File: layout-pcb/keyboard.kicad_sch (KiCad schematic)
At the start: 276 parts

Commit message: pcb basic wiring
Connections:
- net 26p4-27p2: no longer D27.4 (DIN), D28.2 (DOUT)
- net at D66.2 (DOUT): now also D67.4 (DIN)
- net 50p2-66p4: now reaches D66.4 (DIN)
- net 50p2-66p4: now also D50.2 (DOUT)
- net at D69.2 (DOUT): now also D70.4 (DIN)
- net at D69.4 (DIN): now also D68.2 (DOUT)
- net at D92.2 (DOUT): now also D93.4 (DIN)
- net LED-Status IN: now reaches D92.4 (DIN)
- net at D58.2 (DOUT): now also D57.4 (DIN)
- net at D58.4 (DIN): now also D59.2 (DOUT)
- net at D34.2 (DOUT): now also D35.4 (DIN)
- net at D34.4 (DIN): now also D33.2 (DOUT)
- net at D40.2 (DOUT): now also D41.4 (DIN)
- net 39p2-40p4: now reaches D40.4 (DIN)
- net 39p2-40p4: now also D39.2 (DOUT)
- net at D56.2 (DOUT): now also D55.4 (DIN)
- net at D56.4 (DIN): now also D57.2 (DOUT)
- net at D43.2 (DOUT): now also D44.4 (DIN)
- net at D43.4 (DIN): now also D42.2 (DOUT)
- net at D48.2 (DOUT): now also D49.4 (DIN)
- net at D48.4 (DIN): now also D47.2 (DOUT)
- net at D47.4 (DIN): now also D46.2 (DOUT)
- net at D62.2 (DOUT): now also D61.4 (DIN)
- net at D62.4 (DIN): now also D63.2 (DOUT)
- net at D90.2 (DOUT): now also D89.4 (DIN)
- net at D90.4 (DIN): now also D91.2 (DOUT)
- net at D75.2 (DOUT): now also D76.4 (DIN)
- net at D75.4 (DIN): now also D74.2 (DOUT)
- net at D87.2 (DOUT): now also D86.4 (DIN)
- net at D87.4 (DIN): now also D88.2 (DOUT)
- net at D74.4 (DIN): now also D73.2 (DOUT)
- net at D67.2 (DOUT): now also D68.4 (DIN)
- net at D55.2 (DOUT): now also D54.4 (DIN)
- net at D60.2 (DOUT): now also D59.4 (DIN)
- net at D60.4 (DIN): now also D61.2 (DOUT)
- net at D76.2 (DOUT): now also D77.4 (DIN)
- net at D72.2 (DOUT): now also D73.4 (DIN)
- net at D72.4 (DIN): now also D71.2 (DOUT)
- net at D52.2 (DOUT): now also D51.4 (DIN)
- net 53p2-52p4: now reaches D52.4 (DIN)
- net 53p2-52p4: now also D53.2 (DOUT)
- net at D44.2 (DOUT): now also D45.4 (DIN)
- net at D42.4 (DIN): now also D41.2 (DOUT)
- net at D51.2 (DOUT): now also D50.4 (DIN)
- net 81p2-91p4: now reaches D91.4 (DIN)
- net 81p2-91p4: now also D81.2 (DOUT)
- net at D85.2 (DOUT): now also D84.4 (DIN)
- net at D85.4 (DIN): now also D86.2 (DOUT)
- net at D37.2 (DOUT): now also D38.4 (DIN)
- net at D37.4 (DIN): now also D36.2 (DOUT)
- net at D93.2 (DOUT): now also D94.4 (DIN)
- net at D33.4 (DIN): now also D32.2 (DOUT)
- net at D79.2 (DOUT): now also D80.4 (DIN)
- net 78p2-79p4: now reaches D79.4 (DIN)
- net 78p2-79p4: now also D78.2 (DOUT)
- net at D88.4 (DIN): now also D89.2 (DOUT)
- net at D36.4 (DIN): now also D35.2 (DOUT)
- net at D82.4 (DIN): now also D83.2 (DOUT)
- net at D46.4 (DIN): now also D45.2 (DOUT)
- net at D65.2 (DOUT): now also D64.4 (DIN)
- net 49p2-65p4: now reaches D65.4 (DIN)
- net 49p2-65p4: now also D49.2 (DOUT)
- net at D78.4 (DIN): now also D77.2 (DOUT)
- net at D70.2 (DOUT): now also D71.4 (DIN)
- net at D63.4 (DIN): now also D64.2 (DOUT)
- net at D53.4 (DIN): now also D54.2 (DOUT)
- net at D39.4 (DIN): now also D38.2 (DOUT)
- net 14p2-32p4: now reaches D14.2 (DOUT)
- net 14p2-32p4: now also D32.4 (DIN)
- net at D83.4 (DIN): now also D84.2 (DOUT)
- net at D80.2 (DOUT): now also D81.4 (DIN)
- new net: D27.4 (DIN), D28.2 (DOUT)

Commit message: update
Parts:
- removed D1, D10, D11, D12, D13, D14, D15, D16, D17, D18, D19, D2, D20, D21, D22, D23, D24, D25, D26, D27, D28, D29, D3, D30, D31, D32, D33, D34, D35, D36, D37, D38, D39, D4, D40, D41, D42, D43, D44, D45, D46, D47, D48, D49, D5, D50, D51, D52, D53, D54, D55, D56, D57, D58, D59, D6, D60, D61, D62, D63, D64, D65, D66, D67, D68, D69, D7, D70, D71, D72, D73, D74, D75, D76, D77, D78, D79, D8, D80, D81, D82, D83, D84, D85, D86, D87, D88, D89, D9, D90, D91, D92, D93, D94: WS2812B, LED_SMD:LED_WS2812B_PLCC4_5.0x5.0mm_P3.2mm, symbol LED:WS2812B
- D_0, D_1, D_10, D_11, D_12, D_13, D_14, D_15, D_16, D_17, D_18, D_19, D_2, D_20, D_21, D_22, D_23, D_24, D_25, D_26, D_27, D_28, D_29, D_3, D_30, D_31, D_32, D_33, D_34, D_35, D_36, D_37, D_38, D_39, D_4, D_40, D_41, D_42, D_43, D_44, D_45, D_46, D_47, D_48, D_49, D_5, D_50, D_51, D_52, D_53, D_54, D_55, D_56, D_57, D_58, D_59, D_6, D_60, D_61, D_62, D_63, D_64, D_65, D_66, D_67, D_68, D_69, D_7, D_70, D_71, D_72, D_73, D_74, D_75, D_76, D_77, D_78, D_79, D_8, D_80, D_81, D_82, D_83, D_84, D_85, D_86, D_87, D_88, D_89, D_9, D_90: Mouser (none) -> 485-5099
- K_13, K_14, K_15, K_16, K_17, K_18, K_19, K_20, K_21, K_22, K_23, K_24, K_25, K_26, K_27, K_28, K_29, K_30, K_31, K_32, K_33, K_34, K_35, K_36, K_37, K_38, K_39, K_40, K_41, K_42, K_43, K_44, K_45, K_46, K_47, K_48, K_49, K_50, K_51, K_52, K_53, K_54, K_55, K_56, K_57, K_58, K_59, K_60, K_61, K_62, K_63, K_64, K_65, K_66, K_67, K_68, K_69, K_70, K_71, K_72, K_73, K_74, K_75, K_76, K_77, K_78, K_79, K_80, K_81, K_82, K_83, K_84, K_85, K_86, K_87, K_88, K_89, K_90, K_ESC1, K_F1, K_F10, K_F11, K_F12, K_F2, K_F3, K_F4, K_F5, K_F6, K_F7, K_F8, K_F9: Mouser (none) -> 540-MX1A-E1NN
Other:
- added sheet Controler (untitled.kicad_sch)
- added sheet LED Matrix (untitled.kicad_sch)
- company: (none) -> JJW Inc.
- title: (none) -> No Arrows

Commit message: update
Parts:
- added D1, D10, D11, D12, D13, D14, D15, D16, D17, D18, D19, D2, D20, D21, D22, D23, D24, D25, D26, D27, D28, D29, D3, D30, D31, D32, D33, D34, D35, D36, D37, D38, D39, D4, D40, D41, D42, D43, D44, D45, D46, D47, D48, D49, D5, D50, D51, D52, D53, D54, D55, D56, D57, D58, D59, D6, D60, D61, D62, D63, D64, D65, D66, D67, D68, D69, D7, D70, D71, D72, D73, D74, D75, D76, D77, D78, D79, D8, D80, D81, D82, D83, D84, D85, D86, D87, D88, D89, D9, D90, D91, D92, D93, D94: WS2812B, LED_SMD:LED_WS2812B_PLCC4_5.0x5.0mm_P3.2mm, symbol LED:WS2812B
- added J1: USB_C_Receptacle_USB2.0_16P, Connector_USB:USB_C_Receptacle_GCT_USB4110, symbol Connector:USB_C_Receptacle_USB2.0_16P
- added R1, R2: 5K1, Resistor_SMD:R_2010_5025Metric_Pad1.40x2.65mm_HandSolder, symbol Device:R
- added SW1: 3983, kb2040:SW_3983_ADA, symbol 2024-11-03_10-00-00:3983
- added U1: RP2040_Stamp, kb2040:RP2xxx_Stamp_SMD, symbol RP2xxx_Stamp:RP2040_Stamp
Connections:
- net col0: now also U1.30 (GPIO29)
- net col1: now also U1.29 (GPIO28)
- net col10: now also U1.19 (GPIO18)
- net col11: now also U1.18 (GPIO17)
- net col12: now also U1.17 (GPIO16)
- net col13: now also U1.16 (GPIO15)
- net col14: now also U1.15 (GPIO14)
- net col15: now also U1.14 (GPIO13)
- net col16: now also U1.13 (GPIO12)
- net col17: now also U1.12 (GPIO11)
- net col18: now also U1.11 (GPIO10)
- net col2: now also U1.28 (GPIO27)
- net col3: now also U1.27 (GPIO26)
- net col4: now also U1.26 (GPIO25)
- net col5: now also U1.25 (GPIO24)
- net col6: now also U1.24 (GPIO23)
- net col7: now also U1.23 (GPIO22)
- net col8: now also U1.22 (GPIO21)
- net col9: now also U1.21 (GPIO20)
- net row0: now also U1.10 (GPIO9)
- net row1: now also U1.9 (GPIO8)
- net row2: now also U1.8 (GPIO7)
- net row3: now also U1.7 (GPIO6)
- net row4: now also U1.6 (GPIO5)
- net row5: now also U1.5 (GPIO4)
- new net: D6.2 (DOUT), D7.4 (DIN)
- new net: D5.2 (DOUT), D6.4 (DIN)
- new net: D7.2 (DOUT), D8.4 (DIN)
- new net: D23.4 (DIN), D24.2 (DOUT)
- new net: D24.4 (DIN), D25.2 (DOUT)
- new net: D66.2 (DOUT), D67.4 (DIN)
- new net: D17.4 (DIN), D18.2 (DOUT)
- new net: D18.4 (DIN), D19.2 (DOUT)
- new net: J1.A5 (CC1), R1.1
- new net: J1.A4 (VBUS), J1.A9 (VBUS), J1.B4 (VBUS), J1.B9 (VBUS), R1.2, R2.2, U1.33 (5V)
- new net: D69.2 (DOUT), D70.4 (DIN)
- new net: D68.2 (DOUT), D69.4 (DIN)
- new net: D92.2 (DOUT), D93.4 (DIN)
- new net: D57.4 (DIN), D58.2 (DOUT)
- new net: D58.4 (DIN), D59.2 (DOUT)
- new net: D11.2 (DOUT), D12.4 (DIN)
- new net: D10.2 (DOUT), D11.4 (DIN)
- new net: D34.2 (DOUT), D35.4 (DIN)
- new net: D33.2 (DOUT), D34.4 (DIN)
- new net: D29.4 (DIN), D30.2 (DOUT)
- new net: D30.4 (DIN), D31.2 (DOUT)
- new net: D27.4 (DIN), D28.2 (DOUT)
- new net: D40.2 (DOUT), D41.4 (DIN)
- new net: D55.4 (DIN), D56.2 (DOUT)
- new net: D56.4 (DIN), D57.2 (DOUT)
- new net: D43.2 (DOUT), D44.4 (DIN)
- new net: D42.2 (DOUT), D43.4 (DIN)
- new net: D16.4 (DIN), D17.2 (DOUT)
- new net: D48.2 (DOUT), D49.4 (DIN)
- new net: D47.2 (DOUT), D48.4 (DIN)
- new net: D46.2 (DOUT), D47.4 (DIN)
- new net: D1.2 (DOUT), D2.4 (DIN)
- new net: D61.4 (DIN), D62.2 (DOUT)
- new net: D62.4 (DIN), D63.2 (DOUT)
- new net: D89.4 (DIN), D90.2 (DOUT)
- new net: D90.4 (DIN), D91.2 (DOUT)
- new net: D12.2 (DOUT), D13.4 (DIN)
- new net: D75.2 (DOUT), D76.4 (DIN)
- new net: D74.2 (DOUT), D75.4 (DIN)
- new net: D21.4 (DIN), D22.2 (DOUT)
- new net: D22.4 (DIN), D23.2 (DOUT)
- new net: D86.4 (DIN), D87.2 (DOUT)
- new net: D87.4 (DIN), D88.2 (DOUT)
- new net: D73.2 (DOUT), D74.4 (DIN)
- new net: D67.2 (DOUT), D68.4 (DIN)
- new net: D54.4 (DIN), D55.2 (DOUT)
- new net: D59.4 (DIN), D60.2 (DOUT)
- new net: D60.4 (DIN), D61.2 (DOUT)
- new net: D76.2 (DOUT), D77.4 (DIN)
- new net: D72.2 (DOUT), D73.4 (DIN)
- new net: D71.2 (DOUT), D72.4 (DIN)
- new net: D25.4 (DIN), D26.2 (DOUT)
- new net: D51.4 (DIN), D52.2 (DOUT)
- new net: D44.2 (DOUT), D45.4 (DIN)
- new net: D2.2 (DOUT), D3.4 (DIN)
- new net: J1.B5 (CC2), R2.1
- new net: D41.2 (DOUT), D42.4 (DIN)
- new net: D50.4 (DIN), D51.2 (DOUT)
- new net: D28.4 (DIN), D29.2 (DOUT)
- new net: D84.4 (DIN), D85.2 (DOUT)
- new net: D85.4 (DIN), D86.2 (DOUT)
- new net: D3.2 (DOUT), D4.4 (DIN)
- new net: J1.A7 (D-), J1.B7 (D-), U1.35 (USB_D-)
- new net: J1.A6 (D+), J1.B6 (D+), U1.36 (USB_D+)
- new net: SW1.1, U1.40 (BOOTSEL)
- new net: D37.2 (DOUT), D38.4 (DIN)
- new net: D36.2 (DOUT), D37.4 (DIN)
- new net: D93.2 (DOUT), D94.4 (DIN)
- new net: D4.2 (DOUT), D5.4 (DIN)
- new net: D32.2 (DOUT), D33.4 (DIN)
- new net: D79.2 (DOUT), D80.4 (DIN)
- new net: D10.4 (DIN), D9.2 (DOUT)
- new net: D8.2 (DOUT), D9.4 (DIN)
- new net: D88.4 (DIN), D89.2 (DOUT)
- new net: D35.2 (DOUT), D36.4 (DIN)
- new net: D82.4 (DIN), D83.2 (DOUT)
- new net: D45.2 (DOUT), D46.4 (DIN)
- new net: D19.4 (DIN), D20.2 (DOUT)
- new net: D20.4 (DIN), D21.2 (DOUT)
- new net: D64.4 (DIN), D65.2 (DOUT)
- new net: D77.2 (DOUT), D78.4 (DIN)
- new net: D14.4 (DIN), D15.2 (DOUT)
- new net: D15.4 (DIN), D16.2 (DOUT)
- new net: D70.2 (DOUT), D71.4 (DIN)
- new net: D63.4 (DIN), D64.2 (DOUT)
- new net: D53.4 (DIN), D54.2 (DOUT)
- new net: D38.2 (DOUT), D39.4 (DIN)
- new net: D83.4 (DIN), D84.2 (DOUT)
- new net: D80.2 (DOUT), D81.4 (DIN)
- new net 14p2-32p4: D14.2 (DOUT), D32.4 (DIN)
- new net 26p4-27p2: D26.4 (DIN), D27.2 (DOUT)
- new net 31p4 - 13p2: D13.2 (DOUT), D31.4 (DIN)
- new net 39p2-40p4: D39.2 (DOUT), D40.4 (DIN)
- new net 49p2-65p4: D49.2 (DOUT), D65.4 (DIN)
- new net 50p2-66p4: D50.2 (DOUT), D66.4 (DIN)
- new net 53p2-52p4: D52.4 (DIN), D53.2 (DOUT)
- new net 78p2-79p4: D78.2 (DOUT), D79.4 (DIN)
- new net 81p2-91p4: D81.2 (DOUT), D91.4 (DIN)
- new net GND: J1.A1 (GND), J1.A12 (GND), J1.B1 (GND), J1.B12 (GND), SW1.2, U1.31 (GND)
- new net LED-Status IN: D92.4 (DIN)
- new net LED_DTA_IN: D1.4 (DIN)
- new net LED_GND: D1.3 (VSS), D10.3 (VSS), D11.3 (VSS), D12.3 (VSS), D13.3 (VSS), D14.3 (VSS), D15.3 (VSS), D16.3 (VSS), D17.3 (VSS), D18.3 (VSS), D19.3 (VSS), D2.3 (VSS), D20.3 (VSS), D21.3 (VSS), D22.3 (VSS), D23.3 (VSS), D24.3 (VSS), D25.3 (VSS), D26.3 (VSS), D27.3 (VSS), D28.3 (VSS), D29.3 (VSS), D3.3 (VSS), D30.3 (VSS), D31.3 (VSS), D32.3 (VSS), D33.3 (VSS), D34.3 (VSS), D35.3 (VSS), D36.3 (VSS), D37.3 (VSS), D38.3 (VSS), D39.3 (VSS), D4.3 (VSS), D40.3 (VSS), D41.3 (VSS), D42.3 (VSS), D43.3 (VSS), D44.3 (VSS), D45.3 (VSS), D46.3 (VSS), D47.3 (VSS), D48.3 (VSS), D49.3 (VSS), D5.3 (VSS), D50.3 (VSS), D51.3 (VSS), D52.3 (VSS), D53.3 (VSS), D54.3 (VSS), D55.3 (VSS), D56.3 (VSS), D57.3 (VSS), D58.3 (VSS), D59.3 (VSS), D6.3 (VSS), D60.3 (VSS), D61.3 (VSS), D62.3 (VSS), D63.3 (VSS), D64.3 (VSS), D65.3 (VSS), D66.3 (VSS), D67.3 (VSS), D68.3 (VSS), D69.3 (VSS), D7.3 (VSS), D70.3 (VSS), D71.3 (VSS), D72.3 (VSS), D73.3 (VSS), D74.3 (VSS), D75.3 (VSS), D76.3 (VSS), D77.3 (VSS), D78.3 (VSS), D79.3 (VSS), D8.3 (VSS), D80.3 (VSS), D81.3 (VSS), D82.3 (VSS), D83.3 (VSS), D84.3 (VSS), D85.3 (VSS), D86.3 (VSS), D87.3 (VSS), D88.3 (VSS), D89.3 (VSS), D9.3 (VSS), D90.3 (VSS), D91.3 (VSS), D92.3 (VSS), D93.3 (VSS), D94.3 (VSS)
- new net LED_PWR: D1.1 (VDD), D10.1 (VDD), D11.1 (VDD), D12.1 (VDD), D13.1 (VDD), D14.1 (VDD), D15.1 (VDD), D16.1 (VDD), D17.1 (VDD), D18.1 (VDD), D19.1 (VDD), D2.1 (VDD), D20.1 (VDD), D21.1 (VDD), D22.1 (VDD), D23.1 (VDD), D24.1 (VDD), D25.1 (VDD), D26.1 (VDD), D27.1 (VDD), D28.1 (VDD), D29.1 (VDD), D3.1 (VDD), D30.1 (VDD), D31.1 (VDD), D32.1 (VDD), D33.1 (VDD), D34.1 (VDD), D35.1 (VDD), D36.1 (VDD), D37.1 (VDD), D38.1 (VDD), D39.1 (VDD), D4.1 (VDD), D40.1 (VDD), D41.1 (VDD), D42.1 (VDD), D43.1 (VDD), D44.1 (VDD), D45.1 (VDD), D46.1 (VDD), D47.1 (VDD), D48.1 (VDD), D49.1 (VDD), D5.1 (VDD), D50.1 (VDD), D51.1 (VDD), D52.1 (VDD), D53.1 (VDD), D54.1 (VDD), D55.1 (VDD), D56.1 (VDD), D57.1 (VDD), D58.1 (VDD), D59.1 (VDD), D6.1 (VDD), D60.1 (VDD), D61.1 (VDD), D62.1 (VDD), D63.1 (VDD), D64.1 (VDD), D65.1 (VDD), D66.1 (VDD), D67.1 (VDD), D68.1 (VDD), D69.1 (VDD), D7.1 (VDD), D70.1 (VDD), D71.1 (VDD), D72.1 (VDD), D73.1 (VDD), D74.1 (VDD), D75.1 (VDD), D76.1 (VDD), D77.1 (VDD), D78.1 (VDD), D79.1 (VDD), D8.1 (VDD), D80.1 (VDD), D81.1 (VDD), D82.1 (VDD), D83.1 (VDD), D84.1 (VDD), D85.1 (VDD), D86.1 (VDD), D87.1 (VDD), D88.1 (VDD), D89.1 (VDD), D9.1 (VDD), D90.1 (VDD), D91.1 (VDD), D92.1 (VDD), D93.1 (VDD), D94.1 (VDD)
- no-connect marks 0 -> 3
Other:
- removed sheet Controler
- removed sheet LED Matrix
- company: JJW Inc. -> (none)
- title: No Arrows -> (none)

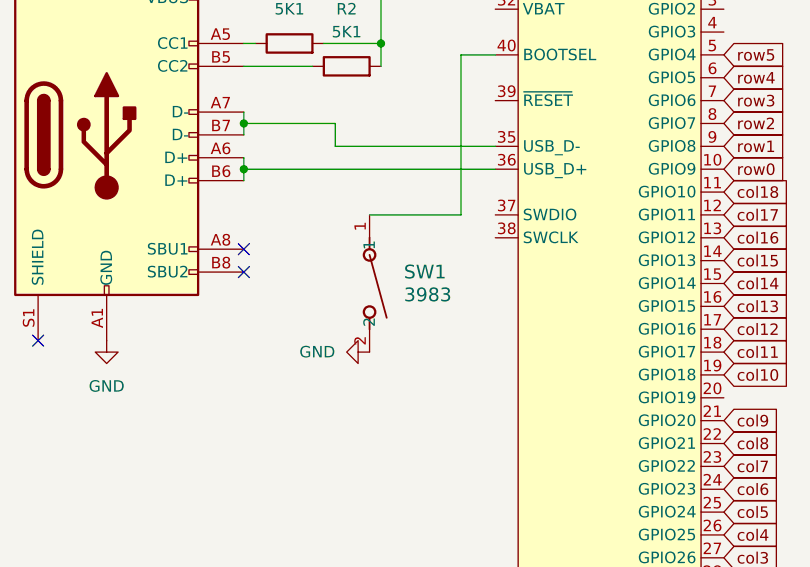
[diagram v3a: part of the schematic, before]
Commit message: LED placemnet #D hotswap and switch
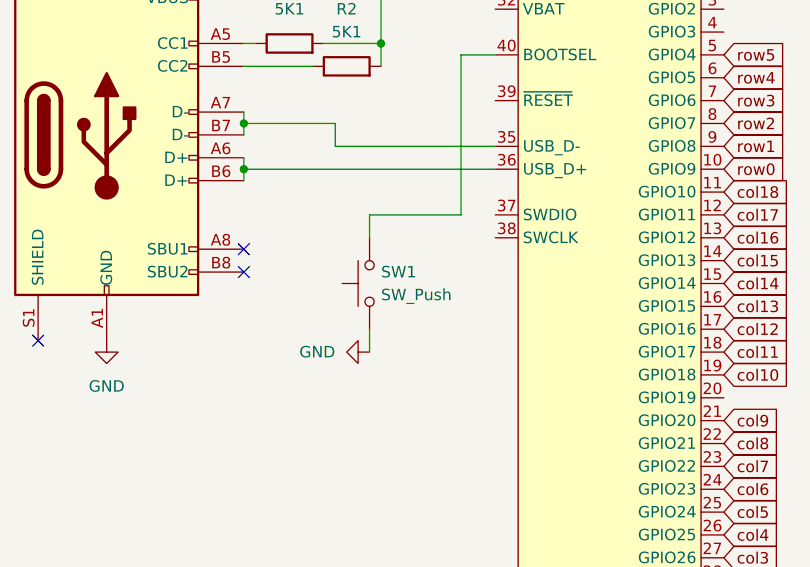
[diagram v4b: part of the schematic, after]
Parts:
- removed SW1: 3983, kb2040:SW_3983_ADA, symbol 2024-11-03_10-00-00:3983
- added SW1: SW_Push, Button_Switch_THT:SW_PUSH_6mm, symbol Switch:SW_Push
- D1, D10, D11, D12, D13, D14, D15, D16, D17, D18, D19, D2, D20, D21, D22, D23, D24, D25, D26, D27, D28, D29, D3, D30, D31, D32, D33, D34, D35, D36, D37, D38, D39, D4, D40, D41, D42, D43, D44, D45, D46, D47, D48, D49, D5, D50, D51, D52, D53, D54, D55, D56, D57, D58, D59, D6, D60, D61, D62, D63, D64, D65, D66, D67, D68, D69, D7, D70, D71, D72, D73, D74, D75, D76, D77, D78, D79, D8, D80, D81, D82, D83, D84, D85, D86, D87, D88, D89, D9, D90, D91, D92, D93, D94: footprint LED_SMD:LED_WS2812B_PLCC4_5.0x5.0mm_P3.2mm -> WS2812-2020:LED_WS2812-2020
- J1: footprint Connector_USB:USB_C_Receptacle_GCT_USB4110 -> Connector_USB:USB_C_Receptacle_G-Switch_GT-USB-7010ASV
- K_ESC1: value KEYSW -> ESC
- R1, R2: footprint Resistor_SMD:R_2010_5025Metric_Pad1.40x2.65mm_HandSolder -> Resistor_SMD:R_01005_0402Metric_Pad0.57x0.30mm_HandSolder
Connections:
- net GND: now also SW1.1
- net at U1.40 (BOOTSEL): now also SW1.2
